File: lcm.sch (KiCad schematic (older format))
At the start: 17 parts, among them J5 1-1734248-5, J6 F52R-1A7H1-11020, U11 NTS0102GT

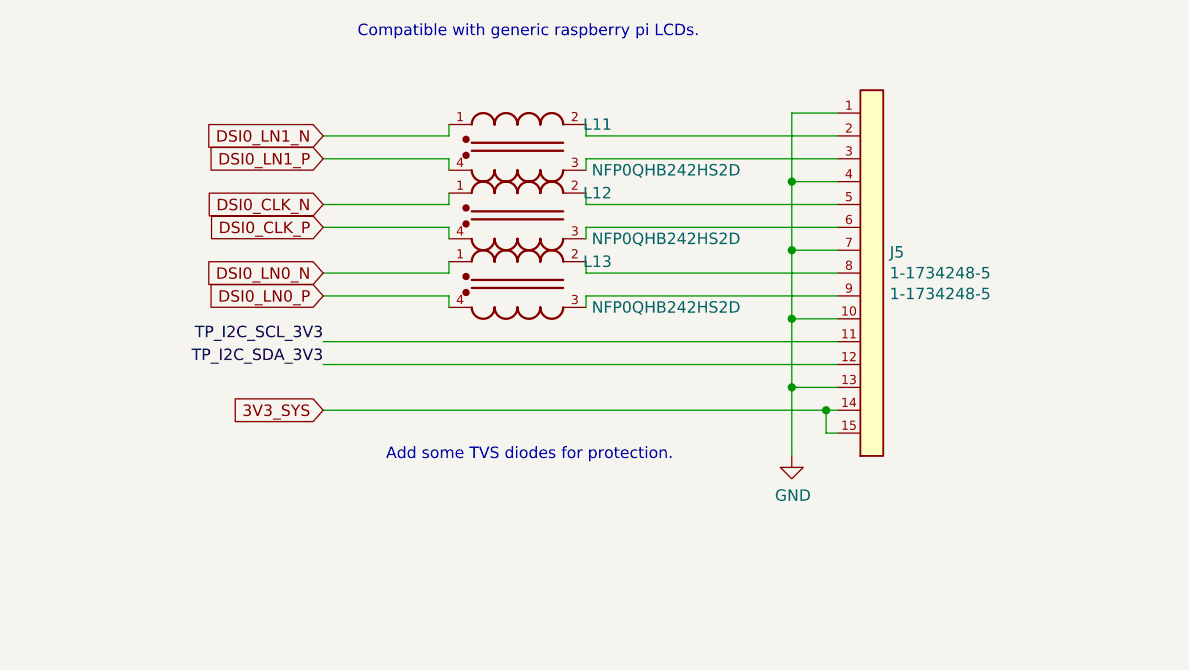
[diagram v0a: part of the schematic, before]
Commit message: Remove 2 lane DSI connector
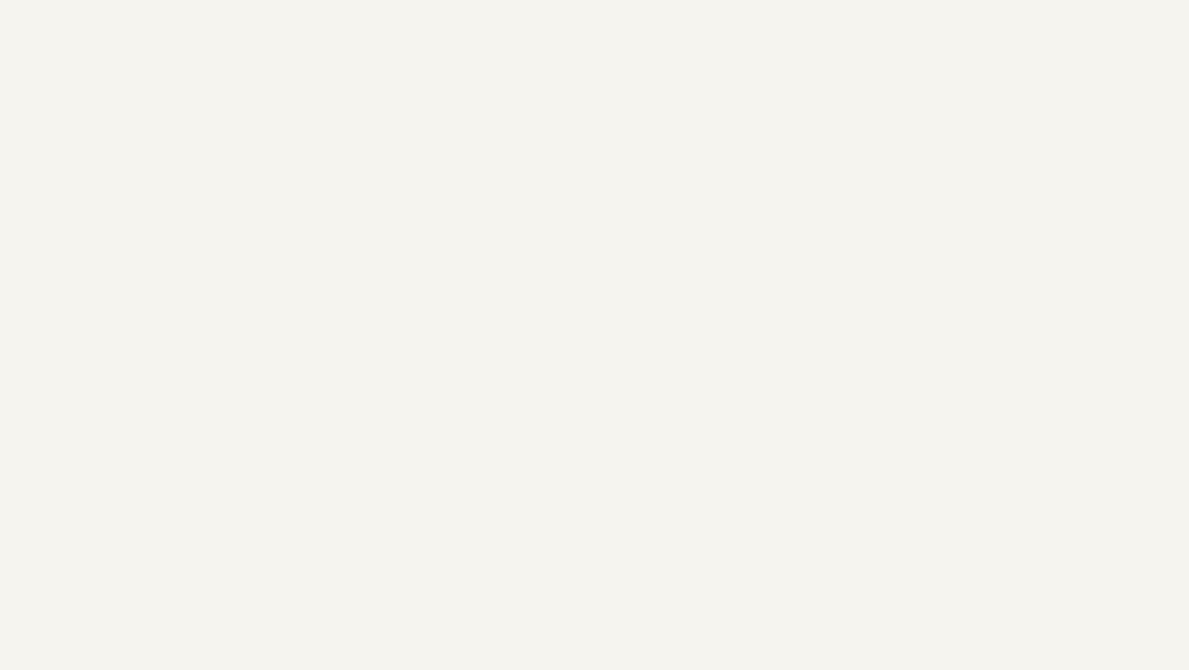
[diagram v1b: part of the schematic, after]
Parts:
- removed J5: 1-1734248-5, sa800u-baseboard-hw-footprints:TE_1-1734248-5, symbol sa800u-baseboard-hw:1-1734248-5
- removed L11, L12, L13: NFP0QHB242HS2D, sa800u-baseboard-hw-footprints:FIL_NFP0QHB242HS2D, symbol sa800u-baseboard-hw:NFP0QHB242HS2D
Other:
- note removed: "Compatible with generic raspberry pi LCDs."
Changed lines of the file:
@@
 $EndDescr
-Wire Wire Line
-	4975 2850 4775 2850
-Wire Wire Line
-	4775 2850 4775 3150
-Wire Wire Line
-	4775 3150 4975 3150
-Wire Wire Line
-	4775 3150 4775 3450
-Wire Wire Line
-	4775 3450 4975 3450
-Connection ~ 4775 3150
-Wire Wire Line
-	4775 3450 4775 3750
-Wire Wire Line
-	4775 3750 4975 3750
-Connection ~ 4775 3450
-Wire Wire Line
-	4775 3750 4775 4050
-Wire Wire Line
-	4775 4050 4975 4050
-Connection ~ 4775 3750
-Wire Wire Line
-	4975 4250 4925 4250
-Wire Wire Line
-	4925 4250 4925 4150
-Wire Wire Line
-	4925 4150 4975 4150
-Wire Wire Line
-	4925 4150 2725 4150
-Connection ~ 4775 4050
-$Comp
-L sa800u-baseboard-hw:GND #PWR063
-U 1 1 61BD6C0B
-P 4775 4350
-F 0 "#PWR063" H 4775 4100 50  0001 C CNN
-F 1 "GND" H 4780 4177 50  0000 C CNN
-F 2 "" H 4775 4350 50  0001 C CNN
-F 3 "" H 4775 4350 50  0001 C CNN
-	1    4775 4350
-	1    0    0    -1
-$EndComp
 Wire Wire Line
 	10500 2900 10250 2900
@@
 	9325 4050 9325 4000
 Wire Wire Line
-	3875 3400 3875 3350
-Wire Wire Line
-	3875 3200 3875 3250
-Wire Wire Line
 	8725 4150 8725 4200
 Wire Wire Line
@@
 Wire Wire Line
 	9325 4350 9325 4300
-Text Notes 2875 2525 0    50   ~ 0
-Compatible with generic raspberry pi LCDs.
 Text Notes 8625 2675 0    50   ~ 0
 General purpose 4 lane DSI for LCD
@@
 	1    0    0    -1
 $EndComp
-$Comp
-L sa800u-baseboard-hw:NFP0QHB242HS2D L?
-U 1 1 61B9B38A
-P 3575 3000
-AR Path="/61B9B38A" Ref="L?"  Part="1"
-AR Path="/61BD2CC1/61B9B38A" Ref="L11"  Part="1"
-F 0 "L11" H 3925 3100 50  0000 C CNN
-F 1 "NFP0QHB242HS2D" H 4225 2900 50  0000 C CNN
-F 2 "sa800u-baseboard-hw-footprints:FIL_NFP0QHB242HS2D" H 3575 3000 50  0001 C CNN
-F 3 "https://www.farnell.com/datasheets/2616945.pdf" H 3575 3000 50  0001 C CNN
-F 4 "NFP0QHB242HS2D" H 3575 3417 50  0001 C CNN "MPN"
-F 5 "MURATA" H 3575 3326 50  0001 C CNN "Manufacturer"
-	1    3575 3000
-	1    0    0    -1
-$EndComp
-Wire Wire Line
-	4975 2950 3875 2950
-Wire Wire Line
-	4975 3050 3875 3050
-Wire Wire Line
-	3875 3050 3875 3100
-Wire Wire Line
-	3875 2950 3875 2900
-Wire Wire Line
-	3275 2900 3275 2950
-Wire Wire Line
-	3275 3100 3275 3050
-$Comp
-L sa800u-baseboard-hw:NFP0QHB242HS2D L?
-U 1 1 61C048CC
-P 3575 3300
-AR Path="/61C048CC" Ref="L?"  Part="1"
-AR Path="/61BD2CC1/61C048CC" Ref="L12"  Part="1"
-F 0 "L12" H 3925 3400 50  0000 C CNN
-F 1 "NFP0QHB242HS2D" H 4225 3200 50  0000 C CNN
-F 2 "sa800u-baseboard-hw-footprints:FIL_NFP0QHB242HS2D" H 3575 3300 50  0001 C CNN
-F 3 "https://www.farnell.com/datasheets/2616945.pdf" H 3575 3300 50  0001 C CNN
-F 4 "NFP0QHB242HS2D" H 3575 3717 50  0001 C CNN "MPN"
-F 5 "MURATA" H 3575 3626 50  0001 C CNN "Manufacturer"
-	1    3575 3300
-	1    0    0    -1
-$EndComp
-Wire Wire Line
-	2725 3050 3275 3050
-Wire Wire Line
-	2725 2950 3275 2950
-Wire Wire Line
-	3875 3250 4975 3250
-Wire Wire Line
-	4975 3350 3875 3350
-Wire Wire Line
-	3275 3400 3275 3350
-Wire Wire Line
-	3275 3350 2725 3350
-Wire Wire Line
-	3275 3200 3275 3250
-Wire Wire Line
-	3275 3250 2725 3250
-$Comp
-L sa800u-baseboard-hw:NFP0QHB242HS2D L?
-U 1 1 61C3A309
-P 3575 3600
-AR Path="/61C3A309" Ref="L?"  Part="1"
-AR Path="/61BD2CC1/61C3A309" Ref="L13"  Part="1"
-F 0 "L13" H 3925 3700 50  0000 C CNN
-F 1 "NFP0QHB242HS2D" H 4225 3500 50  0000 C CNN
-F 2 "sa800u-baseboard-hw-footprints:FIL_NFP0QHB242HS2D" H 3575 3600 50  0001 C CNN
-F 3 "https://www.farnell.com/datasheets/2616945.pdf" H 3575 3600 50  0001 C CNN
-F 4 "NFP0QHB242HS2D" H 3575 4017 50  0001 C CNN "MPN"
-F 5 "MURATA" H 3575 3926 50  0001 C CNN "Manufacturer"
-	1    3575 3600
-	1    0    0    -1
-$EndComp
-Wire Wire Line
-	4975 3550 3875 3550
-Wire Wire Line
-	3875 3550 3875 3500
-Wire Wire Line
-	4975 3650 3875 3650
-Wire Wire Line
-	3875 3650 3875 3700
-Wire Wire Line
-	3275 3500 3275 3550
-Wire Wire Line
-	3275 3550 2725 3550
-Wire Wire Line
-	3275 3700 3275 3650
-Wire Wire Line
-	3275 3650 2725 3650
 $Comp
 L sa800u-baseboard-hw:NFP0QHB242HS2D L?
@@
 	1    0    0    -1
 $EndComp
-Text GLabel 2725 2950 0    50   Input ~ 0
-DSI0_LN1_N
-Text GLabel 2725 3050 0    50   Input ~ 0
-DSI0_LN1_P
-Text GLabel 2725 3250 0    50   Input ~ 0
-DSI0_CLK_N
-Text GLabel 2725 3350 0    50   Input ~ 0
-DSI0_CLK_P
-Text GLabel 2725 3550 0    50   Input ~ 0
-DSI0_LN0_N
-Text GLabel 2725 3650 0    50   Input ~ 0
-DSI0_LN0_P
 Text GLabel 2550 7525 0    50   Input ~ 0
 TP_I2C_SCL
 Text GLabel 2550 7625 0    50   BiDi ~ 0
 TP_I2C_SDA
-Text GLabel 2725 4150 0    50   Input ~ 0
-3V3_SYS
 Text GLabel 8025 3000 0    50   Input ~ 0
 DSI0_LN3_N
@@
 Text GLabel 8025 4800 0    50   Input ~ 0
 3V3_SYS
-Text Notes 3000 4375 0    50   ~ 0
-Add some TVS diodes for protection.
 $Comp
 L sa800u-baseboard-hw:NTS0102GT U11
@@
 Text Label 5325 7625 2    50   ~ 0
 TP_I2C_SDA_3V3
-Text Label 2725 3850 2    50   ~ 0
-TP_I2C_SCL_3V3
-Text Label 2725 3950 2    50   ~ 0
-TP_I2C_SDA_3V3
-Wire Wire Line
-	2725 3850 4975 3850
-Wire Wire Line
-	2725 3950 4975 3950
 Text Label 8025 4600 2    50   ~ 0
 TP_I2C_SDA_3V3
@@
 Wire Wire Line
 	8025 4600 10500 4600
-Connection ~ 4925 4150
-$Comp
-L sa800u-baseboard-hw:1-1734248-5 J5
-U 1 1 66288CCF
-P 5125 3550
-F 0 "J5" H 5203 3641 50  0000 L CNN
-F 1 "1-1734248-5" H 5203 3550 50  0000 L CNN
-F 2 "sa800u-baseboard-hw-footprints:TE_1-1734248-5" H 4675 2250 50  0001 L BNN
-F 3 "https://www.te.com/commerce/DocumentDelivery/DDEController?Action=showdoc&DocId=Customer+Drawing%7F1734248%7FE1%7Fpdf%7FEnglish%7FENG_CD_1734248_E1__.pdf%7F1-1734248-5" H 5275 3550 50  0001 L BNN
-F 4 "TE Connectivity " H 4675 2350 50  0001 L BNN "Manufacturer"
-F 5 "1-1734248-5 " H 5203 3459 50  0000 L CNN "MPN"
-	1    5125 3550
-	1    0    0    -1
-$EndComp
-Wire Wire Line
-	4775 4050 4775 4350
 Text Notes 8450 4925 0    50   ~ 0
 Add some TVS diodes for protection.

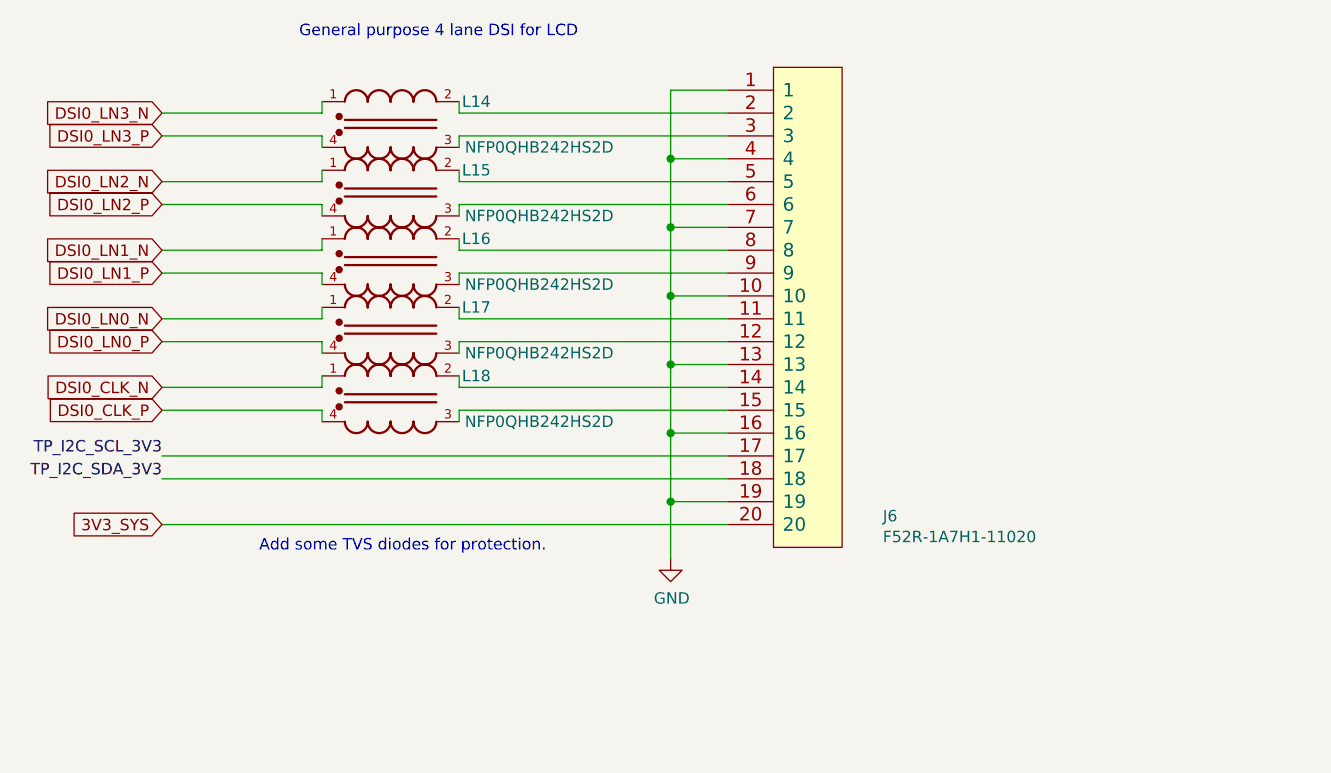
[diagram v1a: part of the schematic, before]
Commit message: Add net labels to dsi signals
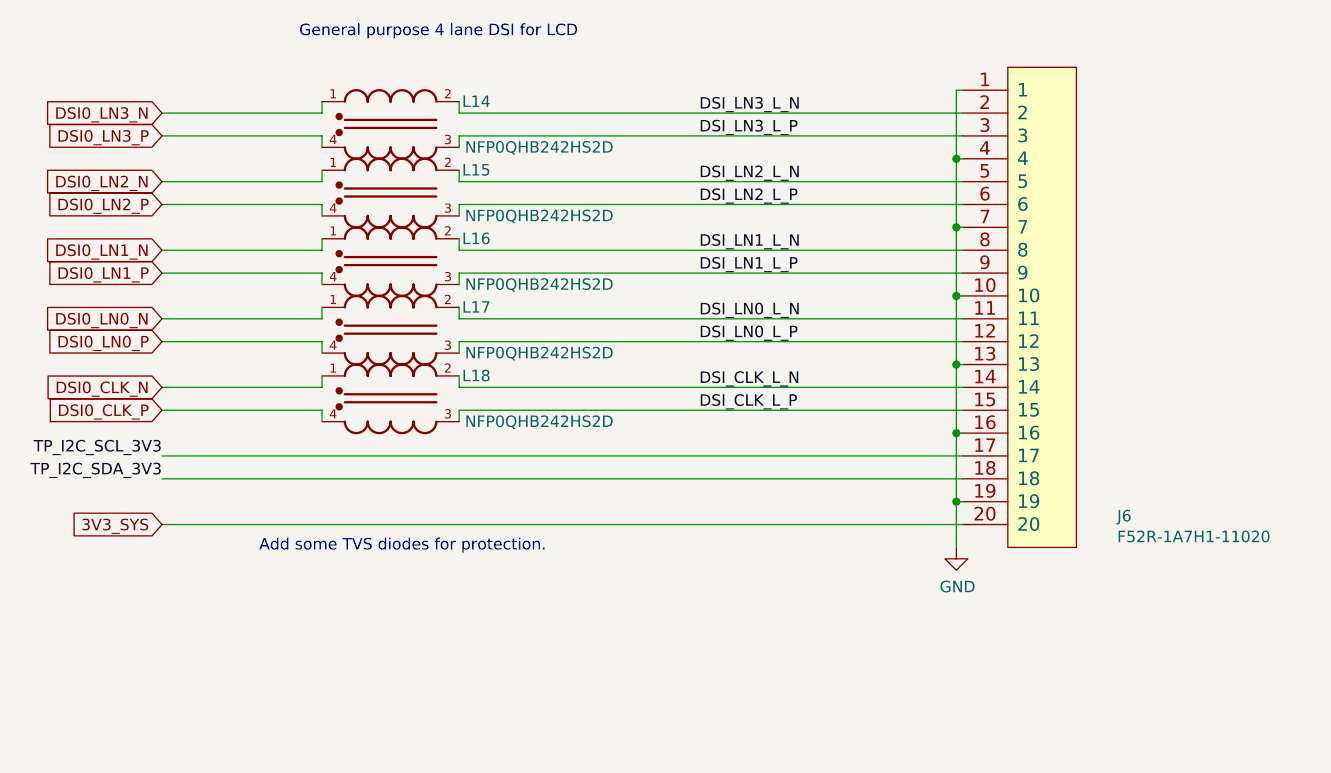
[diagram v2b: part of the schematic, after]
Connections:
- net DSI_LN0_L_N: now reaches J6.11, L17.2
- net DSI_LN0_L_P: now reaches J6.12, L17.3
- net DSI_CLK_L_N: now reaches J6.14, L18.2
- net DSI_CLK_L_P: now reaches J6.15, L18.3
- net DSI_LN3_L_N: now reaches J6.2, L14.2
- net DSI_LN3_L_P: now reaches J6.3, L14.3
- net DSI_LN2_L_N: now reaches J6.5, L15.2
- net DSI_LN2_L_P: now reaches J6.6, L15.3
- net DSI_LN1_L_N: now reaches J6.8, L16.2
- net DSI_LN1_L_P: now reaches J6.9, L16.3
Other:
- moved on the sheet: J6
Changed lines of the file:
@@
 $EndDescr
 Wire Wire Line
-	10500 2900 10250 2900
-Wire Wire Line
-	10250 2900 10250 3200
-Wire Wire Line
-	10250 3200 10500 3200
-Wire Wire Line
-	10250 3200 10250 3500
-Connection ~ 10250 3200
-Wire Wire Line
-	10250 3500 10500 3500
-Connection ~ 10250 3500
-Wire Wire Line
-	10250 3500 10250 3800
-Wire Wire Line
-	10250 3800 10500 3800
-Connection ~ 10250 3800
-Wire Wire Line
-	10250 3800 10250 4100
-Wire Wire Line
-	10250 4100 10500 4100
-Wire Wire Line
-	10250 4100 10250 4400
-Wire Wire Line
-	10250 4400 10500 4400
-Connection ~ 10250 4100
-Wire Wire Line
-	10250 4400 10250 4700
-Wire Wire Line
-	10250 4700 10500 4700
-Connection ~ 10250 4400
-Wire Wire Line
-	8025 4800 10500 4800
-Wire Wire Line
-	10250 4700 10250 4950
-Connection ~ 10250 4700
+	11525 2900 11500 2900
+Wire Wire Line
+	11500 2900 11500 3200
+Wire Wire Line
+	11500 3200 11525 3200
+Wire Wire Line
+	11500 3200 11500 3500
+Connection ~ 11500 3200
+Wire Wire Line
+	11500 3500 11525 3500
+Connection ~ 11500 3500
+Wire Wire Line
+	11500 3500 11500 3800
+Wire Wire Line
+	11500 3800 11525 3800
+Connection ~ 11500 3800
+Wire Wire Line
+	11500 3800 11500 4100
+Wire Wire Line
+	11500 4100 11525 4100
+Wire Wire Line
+	11500 4100 11500 4400
+Wire Wire Line
+	11500 4400 11525 4400
+Connection ~ 11500 4100
+Wire Wire Line
+	11500 4400 11500 4700
+Wire Wire Line
+	11500 4700 11525 4700
+Connection ~ 11500 4400
+Wire Wire Line
+	11500 4700 11500 4900
+Connection ~ 11500 4700
 $Comp
 L sa800u-baseboard-hw:GND #PWR066
 U 1 1 61BEA7A9
-P 10250 4950
-F 0 "#PWR066" H 10250 4700 50  0001 C CNN
-F 1 "GND" H 10255 4777 50  0000 C CNN
-F 2 "" H 10250 4950 50  0001 C CNN
-F 3 "" H 10250 4950 50  0001 C CNN
-	1    10250 4950
+P 11500 4900
+F 0 "#PWR066" H 11500 4650 50  0001 C CNN
+F 1 "GND" H 11505 4727 50  0000 C CNN
+F 2 "" H 11500 4900 50  0001 C CNN
+F 3 "" H 11500 4900 50  0001 C CNN
+	1    11500 4900
 	1    0    0    -1
 $EndComp
@@
 L sa800u-baseboard-hw:F52R-1A7H1-11020 J6
 U 1 1 61ADF1E8
-P 10850 3850
-F 0 "J6" H 11178 2937 50  0000 L CNN
-F 1 "F52R-1A7H1-11020" H 11178 2846 50  0000 L CNN
-F 2 "sa800u-baseboard-hw-footprints:F52R-1A7H1-11020" H 10850 3850 50  0001 C CNN
-F 3 "https://www.snapeda.com/parts/F52R-1A7H1-11020/Amphenol%20ICC%20(FCI)/datasheet/" H 10850 3850 50  0001 C CNN
-F 4 "F52R-1A7H1-11020" H 11178 2755 50  0001 L CNN "MPN"
-F 5 "AMPHENOL ICC" H 11178 2664 50  0001 L CNN "Manufacturer"
-	1    10850 3850
+P 11875 3850
+F 0 "J6" H 12203 2937 50  0000 L CNN
+F 1 "F52R-1A7H1-11020" H 12203 2846 50  0000 L CNN
+F 2 "sa800u-baseboard-hw-footprints:F52R-1A7H1-11020" H 11875 3850 50  0001 C CNN
+F 3 "https://www.snapeda.com/parts/F52R-1A7H1-11020/Amphenol%20ICC%20(FCI)/datasheet/" H 11875 3850 50  0001 C CNN
+F 4 "F52R-1A7H1-11020" H 12203 2755 50  0001 L CNN "MPN"
+F 5 "AMPHENOL ICC" H 12203 2664 50  0001 L CNN "Manufacturer"
+	1    11875 3850
 	1    0    0    -1
 $EndComp
@@
 $EndComp
 Wire Wire Line
-	9325 3000 10500 3000
-Wire Wire Line
-	9325 3100 10500 3100
-Wire Wire Line
-	9325 3300 10500 3300
-Wire Wire Line
-	9325 3400 10500 3400
-Wire Wire Line
-	9325 3600 10500 3600
-Wire Wire Line
-	9325 3700 10500 3700
-Wire Wire Line
-	9325 3900 10500 3900
-Wire Wire Line
-	9325 4000 10500 4000
-Wire Wire Line
-	9325 4200 10500 4200
-Wire Wire Line
-	9325 4300 10500 4300
-Wire Wire Line
-	8025 4500 10500 4500
-Wire Wire Line
-	8025 4600 10500 4600
+	9325 3000 11525 3000
+Wire Wire Line
+	9325 3100 11525 3100
+Wire Wire Line
+	9325 3300 11525 3300
+Wire Wire Line
+	9325 3400 11525 3400
 Text Notes 8450 4925 0    50   ~ 0
 Add some TVS diodes for protection.
+Wire Wire Line
+	8025 4800 11525 4800
+Wire Wire Line
+	8025 4600 11525 4600
+Wire Wire Line
+	8025 4500 11525 4500
+Wire Wire Line
+	9325 4300 11525 4300
+Wire Wire Line
+	9325 4200 11525 4200
+Wire Wire Line
+	9325 4000 11525 4000
+Wire Wire Line
+	9325 3900 11525 3900
+Wire Wire Line
+	9325 3700 11525 3700
+Wire Wire Line
+	9325 3600 11525 3600
+Text Label 10375 3000 0    50   ~ 0
+DSI_LN3_L_N
+Text Label 10375 3100 0    50   ~ 0
+DSI_LN3_L_P
+Text Label 10375 3300 0    50   ~ 0
+DSI_LN2_L_N
+Text Label 10375 3400 0    50   ~ 0
+DSI_LN2_L_P
+Text Label 10375 3600 0    50   ~ 0
+DSI_LN1_L_N
+Text Label 10375 3700 0    50   ~ 0
+DSI_LN1_L_P
+Text Label 10375 3900 0    50   ~ 0
+DSI_LN0_L_N
+Text Label 10375 4000 0    50   ~ 0
+DSI_LN0_L_P
+Text Label 10375 4200 0    50   ~ 0
+DSI_CLK_L_N
+Text Label 10375 4300 0    50   ~ 0
+DSI_CLK_L_P
 $EndSCHEMATC

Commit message: Fix labels
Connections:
- net DSI0_CLK_N: now also L18.2; no longer L18.1
- net DSI0_CLK_P: now also L18.3; no longer L18.4
- net DSI0_LN0_N: now also L17.2; no longer L17.1
- net DSI0_LN0_P: now also L17.3; no longer L17.4
- net DSI0_LN1_N: now also L16.2; no longer L16.1
- net DSI0_LN1_P: now also L16.3; no longer L16.4
- net DSI0_LN2_N: now also L15.2; no longer L15.1
- net DSI0_LN2_P: now also L15.3; no longer L15.4
- net DSI0_LN3_N: now also L14.2; no longer L14.1
- net DSI0_LN3_P: now also L14.3; no longer L14.4
- net DSI_CLK_L_N: now also L18.1; no longer L18.2
- net DSI_CLK_L_P: now also L18.4; no longer L18.3
- net DSI_LN0_L_N: now also L17.1; no longer L17.2
- net DSI_LN0_L_P: now also L17.4; no longer L17.3
- net DSI_LN1_L_N: now also L16.1; no longer L16.2
- net DSI_LN1_L_P: now also L16.4; no longer L16.3
- net DSI_LN2_L_N: now also L15.1; no longer L15.2
- net DSI_LN2_L_P: now also L15.4; no longer L15.3
- net DSI_LN3_L_N: now also L14.1; no longer L14.2
- net DSI_LN3_L_P: now also L14.4; no longer L14.3
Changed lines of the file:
@@
 F 5 "MURATA" H 9025 3676 50  0001 C CNN "Manufacturer"
 	1    9025 3350
-	1    0    0    -1
+	-1   0    0    -1
 $EndComp
 $Comp
@@
 F 5 "MURATA" H 9025 3976 50  0001 C CNN "Manufacturer"
 	1    9025 3650
-	1    0    0    -1
+	-1   0    0    -1
 $EndComp
 $Comp
@@
 F 5 "MURATA" H 9025 4276 50  0001 C CNN "Manufacturer"
 	1    9025 3950
-	1    0    0    -1
+	-1   0    0    -1
 $EndComp
 $Comp
@@
 F 5 "MURATA" H 9025 4576 50  0001 C CNN "Manufacturer"
 	1    9025 4250
-	1    0    0    -1
+	-1   0    0    -1
 $EndComp
 Text GLabel 2550 7525 0    50   Input ~ 0
@@
 F 5 "MURATA" H 9025 3376 50  0001 C CNN "Manufacturer"
 	1    9025 3050
-	1    0    0    -1
-$EndComp
-Wire Wire Line
+	-1   0    0    -1
+$EndComp
+Wire Wire Line

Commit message: Cleanup
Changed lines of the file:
@@
 $Descr A3 16535 11693
 encoding utf-8
-Sheet 5 13
+Sheet 5 12
 Title ""
 Date ""
@@
 Text Label 5325 7625 2    50   ~ 0
 TP_I2C_SDA_3V3
-Text Label 8025 4600 2    50   ~ 0
+Text Label 7550 4600 0    50   ~ 0
 TP_I2C_SDA_3V3
-Text Label 8025 4500 2    50   ~ 0
+Text Label 7550 4500 0    50   ~ 0
 TP_I2C_SCL_3V3
 $Comp
@@
 	8025 4800 11525 4800
 Wire Wire Line
-	8025 4600 11525 4600
-Wire Wire Line
-	8025 4500 11525 4500
+	7550 4600 11525 4600
+Wire Wire Line
+	7550 4500 11525 4500
 Wire Wire Line
 	9325 4300 11525 4300
